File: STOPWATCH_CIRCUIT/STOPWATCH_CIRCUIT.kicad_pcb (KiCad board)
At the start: 2 copper layers, 48 x 77.5 mm, 21 parts, among them SW1 SW_START, SW2 SW_STOP, SW3 SW_RESET, SW4 SW_SPDT, U1 74AHC595, U2 LTC-4627JD, U3 TC1017-xCT

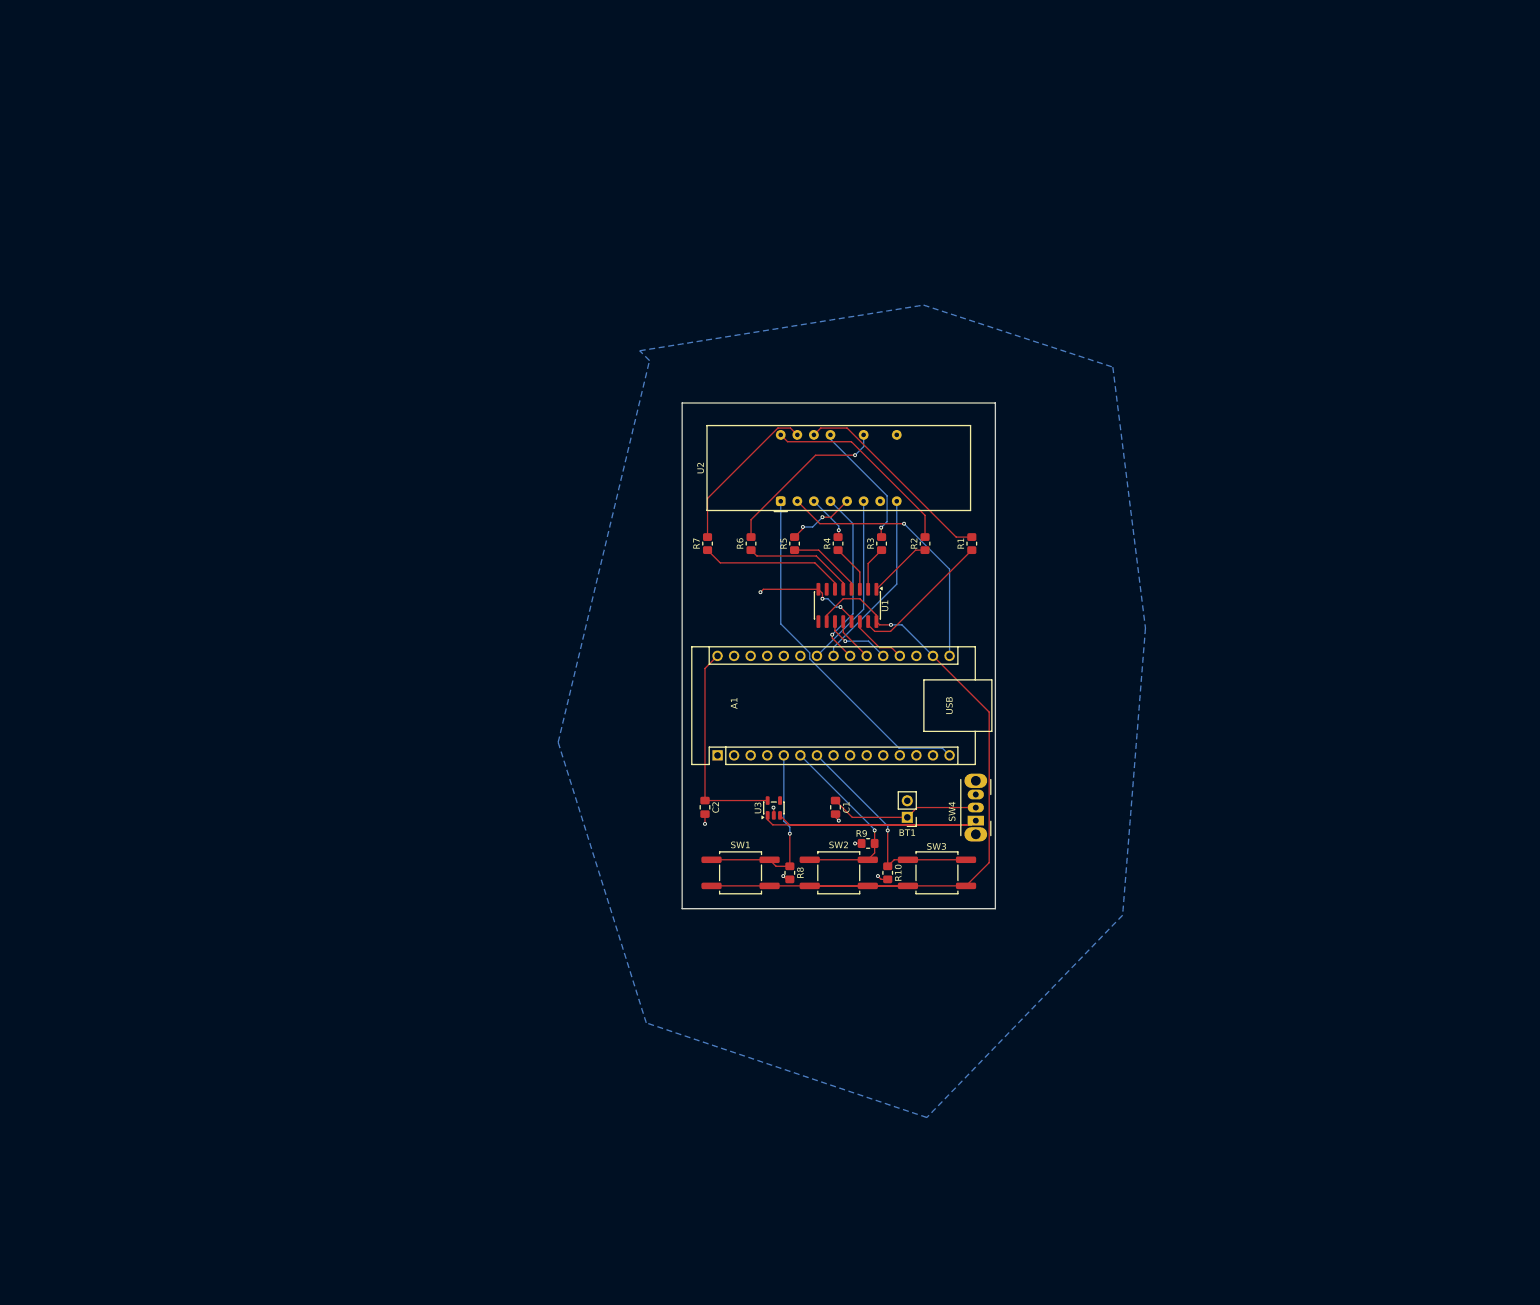
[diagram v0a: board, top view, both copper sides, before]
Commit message: Finished adding the 2 extra digits for miliseconds and redid the whole board
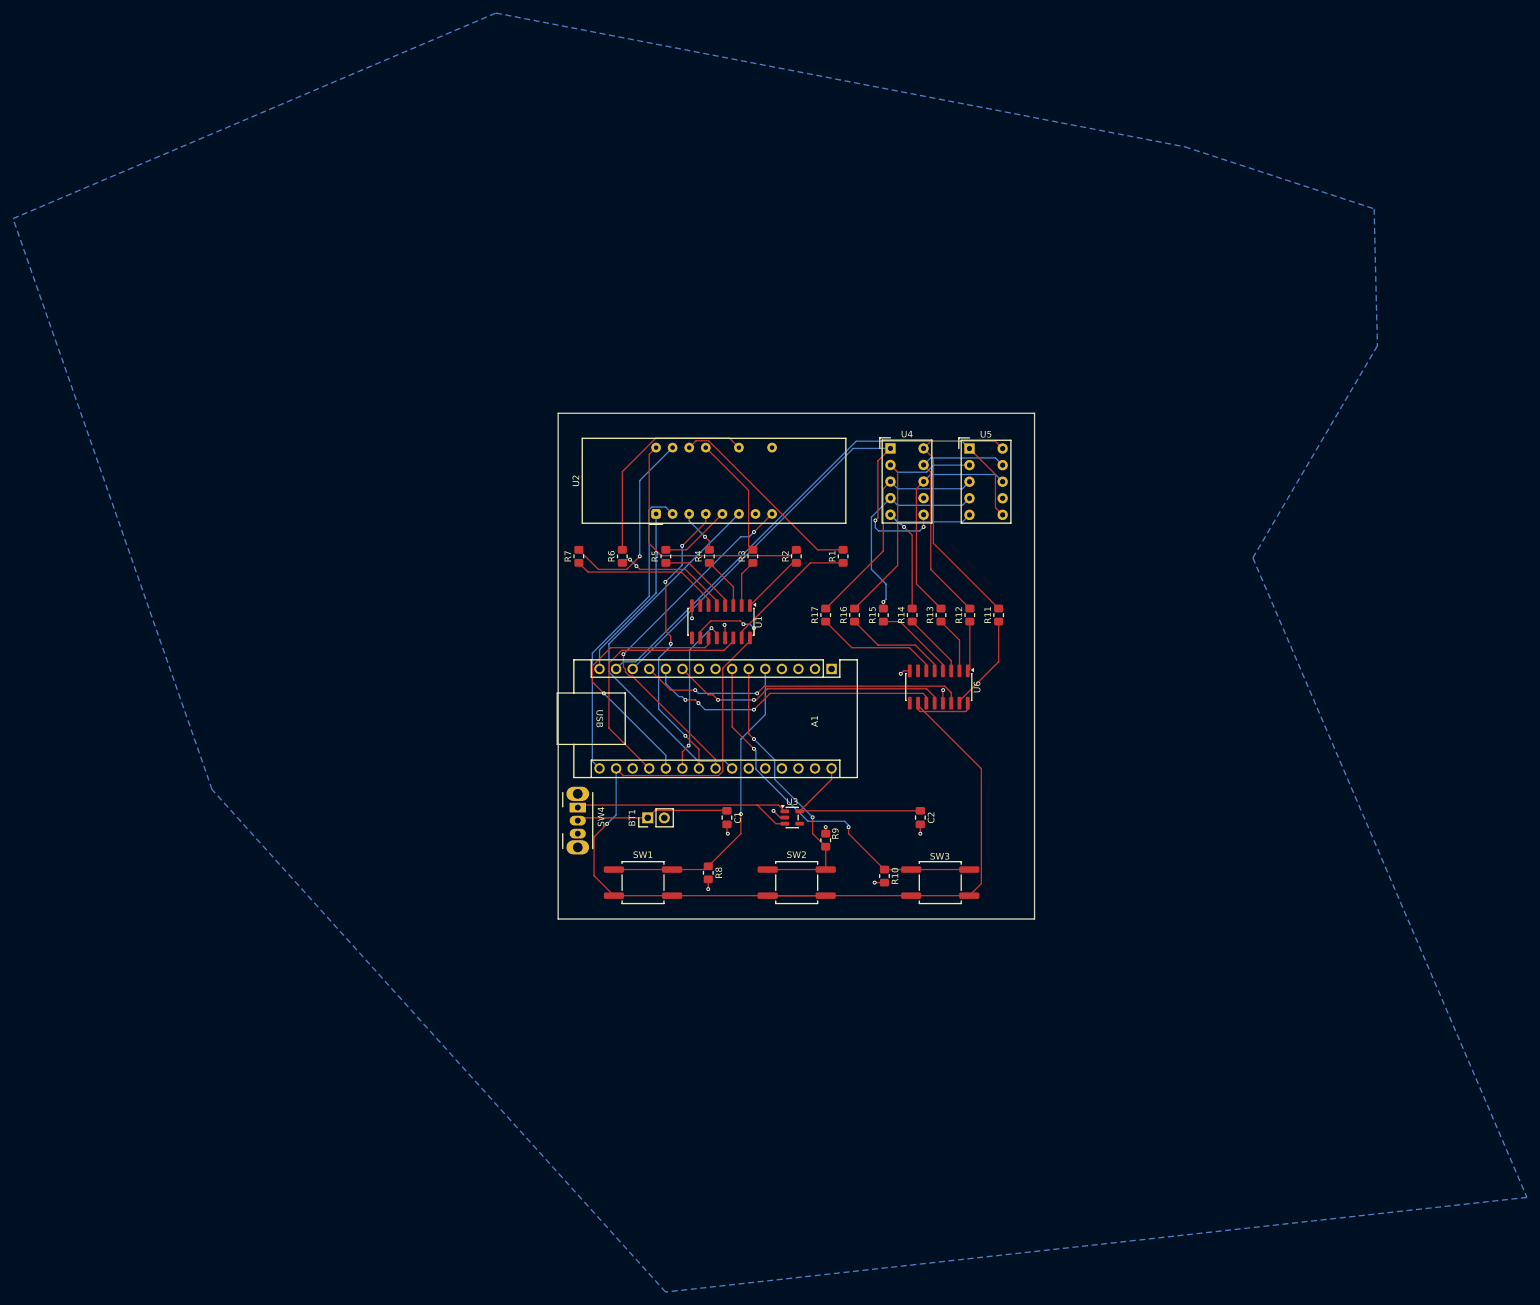
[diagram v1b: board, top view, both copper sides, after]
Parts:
- added R11: 470R, Resistor_SMD:R_0805_2012Metric_Pad1.20x1.40mm_HandSolder, F.Cu at (158.0, 80.5)
- added R12: 470R, Resistor_SMD:R_0805_2012Metric_Pad1.20x1.40mm_HandSolder, F.Cu at (153.6, 80.5)
- added R13: 470R, Resistor_SMD:R_0805_2012Metric_Pad1.20x1.40mm_HandSolder, F.Cu at (149.2, 80.5)
- added R14: 470R, Resistor_SMD:R_0805_2012Metric_Pad1.20x1.40mm_HandSolder, F.Cu at (144.8, 80.5)
- added R15: 470R, Resistor_SMD:R_0805_2012Metric_Pad1.20x1.40mm_HandSolder, F.Cu at (140.3, 80.5)
- added R16: 470R, Resistor_SMD:R_0805_2012Metric_Pad1.20x1.40mm_HandSolder, F.Cu at (135.9, 80.5)
- added R17: 470R, Resistor_SMD:R_0805_2012Metric_Pad1.20x1.40mm_HandSolder, F.Cu at (131.5, 80.5)
- added U4: HDSP-7801, Display_7Segment:HDSP-7801, F.Cu at (141.4, 55.0)
- added U5: HDSP-7801, Display_7Segment:HDSP-7801, F.Cu at (153.5, 55.0)
- added U6: 74AHC595, Package_SO:SOIC-16_3.9x9.9mm_P1.27mm, F.Cu at (148.8, 91.5)
- moved SW4 61.0 mm to (93.5, 110.0), turned to -90 degrees
- moved BT1 39.8 mm to (104.2, 111.6), turned to 90 degrees
- moved C2 33.0 mm to (146.0, 111.5)
- moved A1 21.9 mm to (132.4, 88.8), turned to -90 degrees
- moved R3 19.8 mm to (120.3, 71.5)
- moved R6 19.8 mm to (100.3, 71.5)
- moved R1 19.8 mm to (134.2, 71.5)
- moved R2 19.8 mm to (127.0, 71.5)
- moved R5 19.8 mm to (107.0, 71.5)
- moved R7 19.8 mm to (93.7, 71.5)
- moved R4 19.8 mm to (113.7, 71.5)
- moved U1 19.5 mm to (115.4, 81.5)
- moved U2 19.2 mm to (105.5, 65.0)
- moved C1 16.7 mm to (116.4, 111.5)
- moved SW1 15.0 mm to (103.5, 121.5)
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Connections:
- A1 pad 10: unconnected-(A1-D7-Pad10) -> Net-(A1-D7)
- A1 pad 11: unconnected-(A1-D8-Pad11) -> Net-(A1-D8)
- A1 pad 12: unconnected-(A1-D9-Pad12) -> Net-(A1-D9)
- A1 pad 13: unconnected-(A1-D10-Pad13) -> Net-(A1-D10)
- A1 pad 14: unconnected-(A1-D11-Pad14) -> Net-(A1-D11)
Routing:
- net Net-(A1-D11): track 0.00 -> 81.3 mm
- net Net-(A1-D10): track 0.00 -> 76.3 mm, vias 0 -> 2
- net VCC: track 123.0 -> 181.0 mm, vias 1 -> 3
- net Net-(A1-D9): track 0.00 -> 50.3 mm, vias 0 -> 2
- net Net-(A1-D8): track 0.00 -> 46.0 mm, vias 0 -> 3
- net Net-(A1-D7): track 0.00 -> 42.8 mm, vias 0 -> 2
- net Net-(U4-A): track 0.00 -> 42.3 mm
- net Net-(U4-F): track 0.00 -> 38.2 mm
- net Net-(U4-B): track 0.00 -> 37.9 mm
- net Net-(U4-G): track 0.00 -> 36.6 mm
- net Net-(U4-C): track 0.00 -> 34.5 mm
- net Net-(U4-E): track 0.00 -> 32.2 mm, vias 0 -> 1
- net Net-(A1-A5): track 26.7 -> 57.5 mm
- net Net-(A1-A0): track 8.88 -> 39.6 mm
- net Net-(A1-A1): track 10.4 -> 40.5 mm
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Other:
- board size 48 x 77.5 mm -> 73 x 77.5 mm
